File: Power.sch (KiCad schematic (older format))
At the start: 17 parts

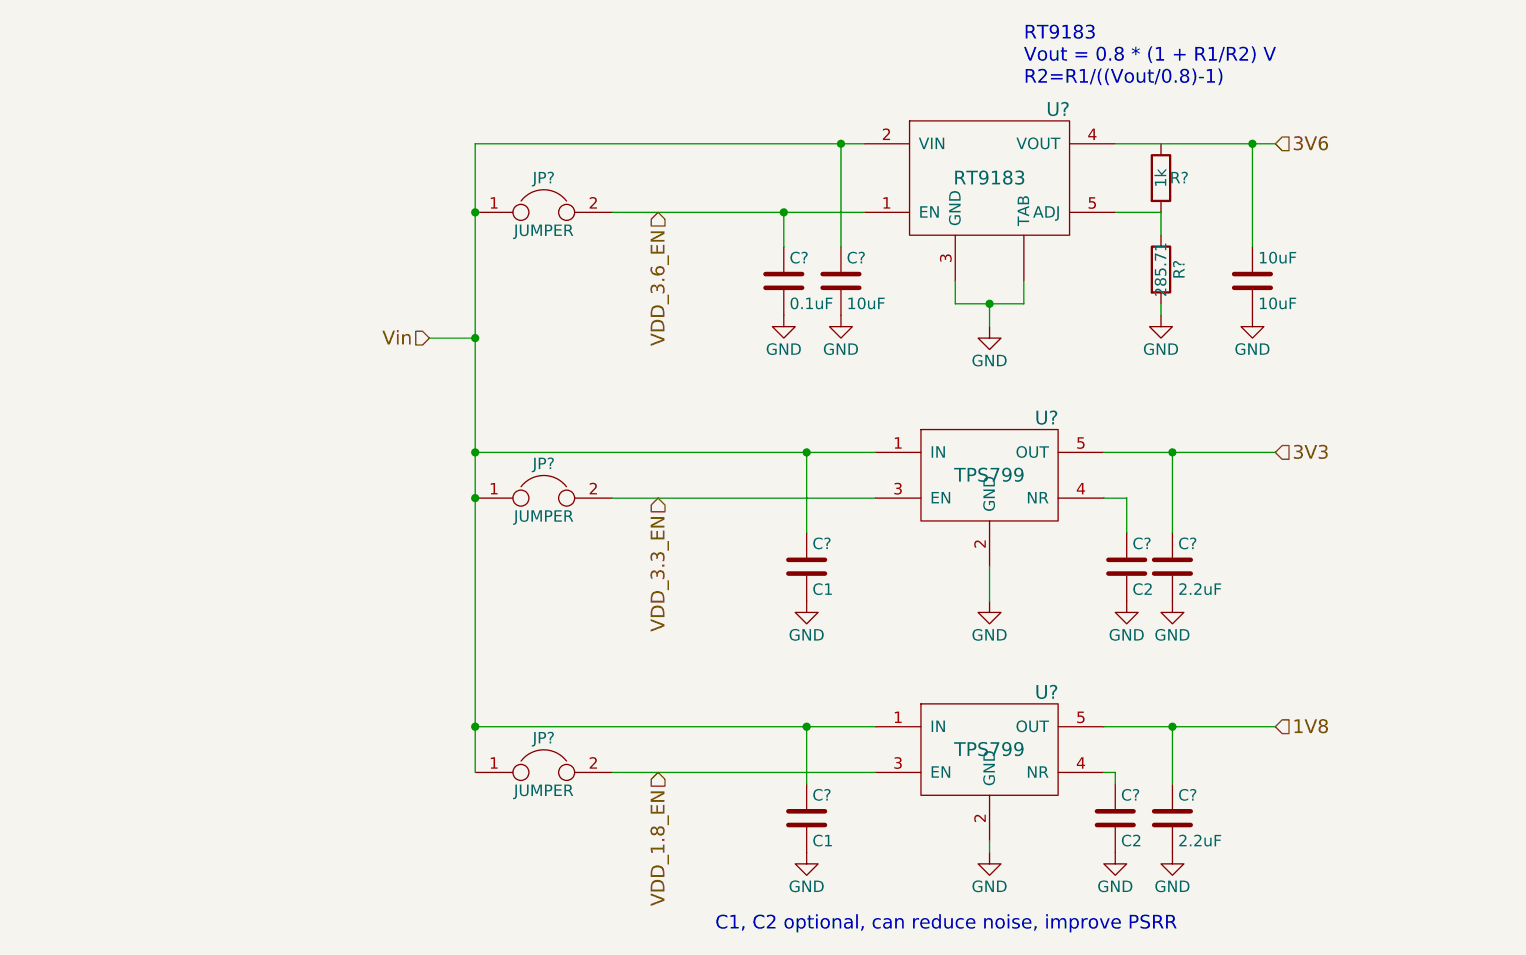
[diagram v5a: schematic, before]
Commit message: added switches for various option and nmos array to control status leds
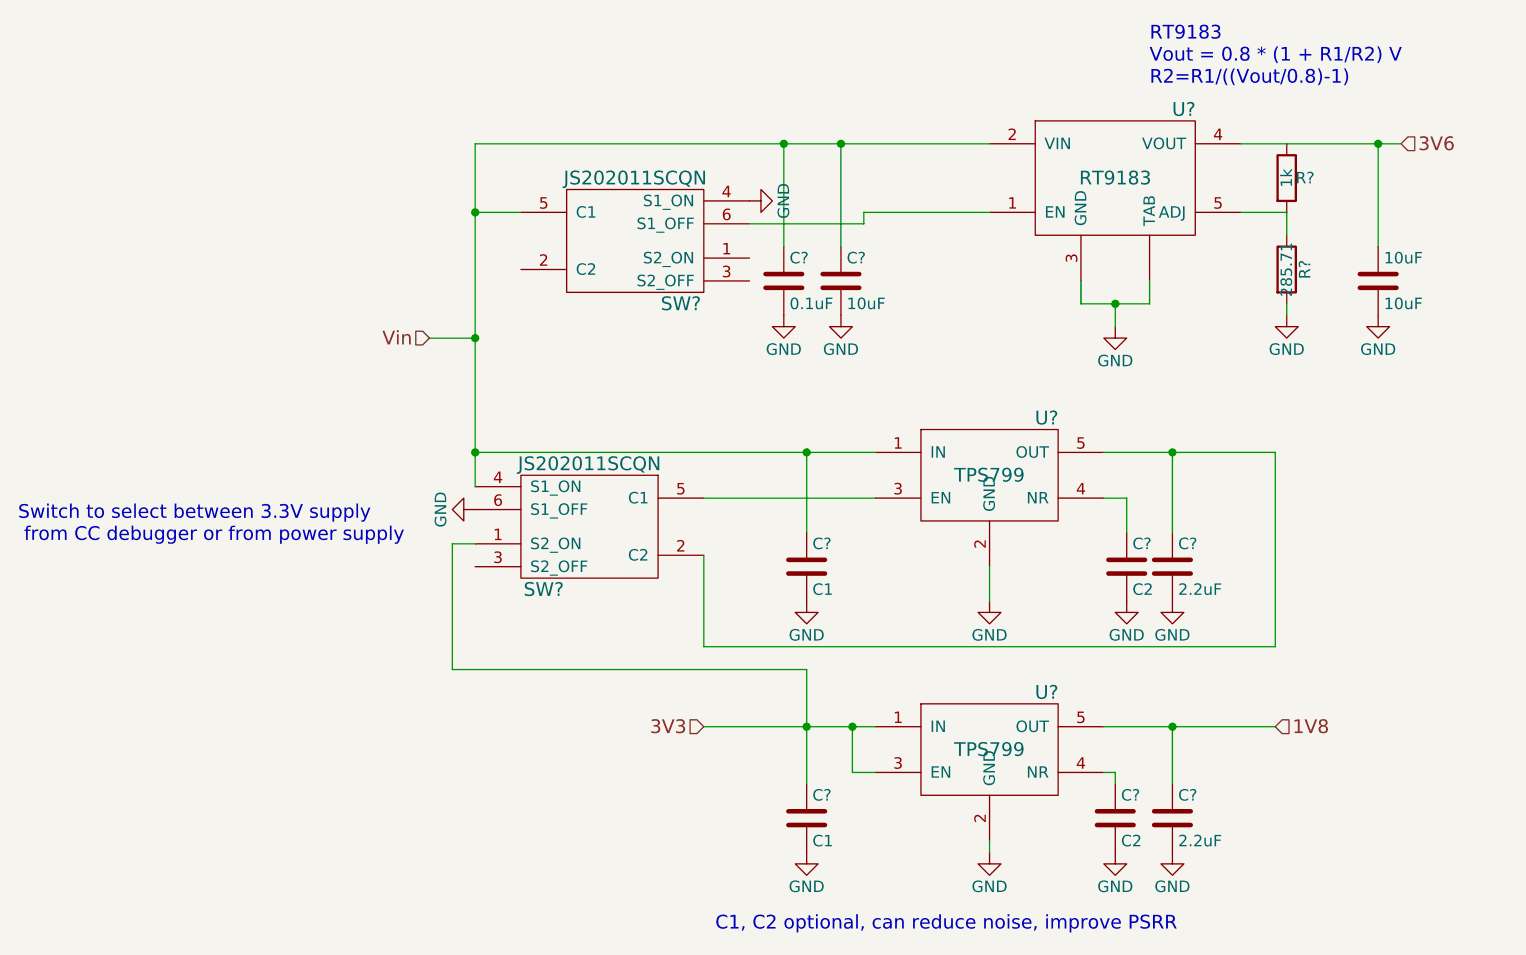
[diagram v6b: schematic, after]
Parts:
- removed JP? (x3): JUMPER, symbol JUMPER
- added SW? (x2): JS202011SCQN, symbol JS202011SCQN
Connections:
- net VDD_1.8_EN is gone; now on net 3V3: U?.3 (EN)
- net 3V3: now also C?.1, U?.1 (IN), SW?.1 (S2_ON); no longer C?.1, U?.5 (OUT)
- net GND: now also SW?.4 (S1_ON), SW?.6 (S1_OFF)
- net Vin: now also C?.1, SW?.4 (S1_ON), SW?.5 (C1); no longer C?.1, U?.1 (IN)
- net VDD_3.3_EN: no longer names the net of U?.3 (EN)
- net VDD_3.3_EN: now also SW?.5 (C1)
- net VDD_3.6_EN: no longer names the net of U?.1 (EN)
- net VDD_3.6_EN: now also SW?.6 (S1_OFF); no longer C?.1
- new net: C?.1, SW?.2 (C2), U?.5 (OUT)
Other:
- note added: "Switch to select between 3.3V supply\n from CC debugger or from power supply\n"
- moved on the sheet: 10uF, R?, U?
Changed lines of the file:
@@
 Text HLabel 3900 2850 0    60   Input ~ 0
 Vin
-Text HLabel 7600 3350 2    60   Input ~ 0
+Text HLabel 5100 4550 0    60   Input ~ 0
 3V3
-Text HLabel 7600 2000 2    60   Input ~ 0
+Text HLabel 8150 2000 2    60   Input ~ 0
 3V6
 Text HLabel 7600 4550 2    60   Input ~ 0
@@
 L RT9183 U?
 U 1 1 58770580
-P 6350 2150
-F 0 "U?" H 6650 2450 60  0000 C CNN
-F 1 "RT9183" H 6350 2150 60  0000 C CNN
-F 2 "" H 6350 2150 60  0001 C CNN
-F 3 "" H 6350 2150 60  0001 C CNN
-	1    6350 2150
+P 6900 2150
+F 0 "U?" H 7200 2450 60  0000 C CNN
+F 1 "RT9183" H 6900 2150 60  0000 C CNN
+F 2 "" H 6900 2150 60  0001 C CNN
+F 3 "" H 6900 2150 60  0001 C CNN
+	1    6900 2150
 	1    0    0    -1
 $EndComp
@@
 L GND #PWR?
 U 1 1 58770941
-P 6350 2800
-F 0 "#PWR?" H 6350 2550 50  0001 C CNN
-F 1 "GND" H 6350 2650 50  0000 C CNN
-F 2 "" H 6350 2800 50  0000 C CNN
-F 3 "" H 6350 2800 50  0000 C CNN
-	1    6350 2800
+P 6900 2800
+F 0 "#PWR?" H 6900 2550 50  0001 C CNN
+F 1 "GND" H 6900 2650 50  0000 C CNN
+F 2 "" H 6900 2800 50  0000 C CNN
+F 3 "" H 6900 2800 50  0000 C CNN
+	1    6900 2800
 	1    0    0    -1
 $EndComp
@@
 L C 10uF
 U 1 1 58770AC4
-P 7500 2600
-F 0 "10uF" H 7525 2700 50  0000 L CNN
-F 1 "10uF" H 7525 2500 50  0000 L CNN
-F 2 "" H 7538 2450 50  0000 C CNN
-F 3 "" H 7500 2600 50  0000 C CNN
-	1    7500 2600
+P 8050 2600
+F 0 "10uF" H 8075 2700 50  0000 L CNN
+F 1 "10uF" H 8075 2500 50  0000 L CNN
+F 2 "" H 8088 2450 50  0000 C CNN
+F 3 "" H 8050 2600 50  0000 C CNN
+	1    8050 2600
 	1    0    0    -1
 $EndComp
@@
 L GND #PWR?
 U 1 1 58770B93
-P 7500 2750
-F 0 "#PWR?" H 7500 2500 50  0001 C CNN
-F 1 "GND" H 7500 2600 50  0000 C CNN
-F 2 "" H 7500 2750 50  0000 C CNN
-F 3 "" H 7500 2750 50  0000 C CNN
-	1    7500 2750
+P 8050 2750
+F 0 "#PWR?" H 8050 2500 50  0001 C CNN
+F 1 "GND" H 8050 2600 50  0000 C CNN
+F 2 "" H 8050 2750 50  0000 C CNN
+F 3 "" H 8050 2750 50  0000 C CNN
+	1    8050 2750
 	1    0    0    -1
 $EndComp
@@
 L GND #PWR?
 U 1 1 58770BD7
-P 7100 2750
-F 0 "#PWR?" H 7100 2500 50  0001 C CNN
-F 1 "GND" H 7100 2600 50  0000 C CNN
-F 2 "" H 7100 2750 50  0000 C CNN
-F 3 "" H 7100 2750 50  0000 C CNN
-	1    7100 2750
+P 7650 2750
+F 0 "#PWR?" H 7650 2500 50  0001 C CNN
+F 1 "GND" H 7650 2600 50  0000 C CNN
+F 2 "" H 7650 2750 50  0000 C CNN
+F 3 "" H 7650 2750 50  0000 C CNN
+	1    7650 2750
 	1    0    0    -1
 $EndComp
@@
 L R R?
 U 1 1 58770EF4
-P 7100 2550
-F 0 "R?" V 7180 2550 50  0000 C CNN
-F 1 "285.71" V 7100 2550 50  0000 C CNN
-F 2 "" V 7030 2550 50  0000 C CNN
-F 3 "" H 7100 2550 50  0000 C CNN
-	1    7100 2550
+P 7650 2550
+F 0 "R?" V 7730 2550 50  0000 C CNN
+F 1 "285.71" V 7650 2550 50  0000 C CNN
+F 2 "" V 7580 2550 50  0000 C CNN
+F 3 "" H 7650 2550 50  0000 C CNN
+	1    7650 2550
 	1    0    0    -1
 $EndComp
@@
 L R R?
 U 1 1 58770EC5
-P 7100 2150
-F 0 "R?" H 7180 2150 50  0000 C CNN
-F 1 "1k" V 7100 2150 50  0000 C CNN
-F 2 "" V 7030 2150 50  0000 C CNN
-F 3 "" H 7100 2150 50  0000 C CNN
-	1    7100 2150
-	1    0    0    -1
-$EndComp
-Text Notes 6500 1750 0    60   ~ 0
+P 7650 2150
+F 0 "R?" H 7730 2150 50  0000 C CNN
+F 1 "1k" V 7650 2150 50  0000 C CNN
+F 2 "" V 7580 2150 50  0000 C CNN
+F 3 "" H 7650 2150 50  0000 C CNN
+	1    7650 2150
+	1    0    0    -1
+$EndComp
+Text Notes 7050 1750 0    60   ~ 0
 RT9183\nVout = 0.8 * (1 + R1/R2) V\nR2=R1/((Vout/0.8)-1)
 $Comp
@@
 Text Notes 5150 5450 0    60   ~ 0
 C1, C2 optional, can reduce noise, improve PSRR
-Text HLabel 4900 4750 3    60   Input ~ 0
-VDD_1.8_EN
-Text HLabel 4900 3550 3    60   Input ~ 0
-VDD_3.3_EN
-Text HLabel 4900 2300 3    60   Input ~ 0
-VDD_3.6_EN
-$Comp
-L JUMPER JP?
-U 1 1 587BADC1
-P 4400 2300
-F 0 "JP?" H 4400 2450 50  0000 C CNN
-F 1 "JUMPER" H 4400 2220 50  0000 C CNN
-F 2 "" H 4400 2300 50  0000 C CNN
-F 3 "" H 4400 2300 50  0000 C CNN
-	1    4400 2300
-	1    0    0    -1
-$EndComp
-$Comp
-L JUMPER JP?
-U 1 1 587BAE6A
-P 4400 3550
-F 0 "JP?" H 4400 3700 50  0000 C CNN
-F 1 "JUMPER" H 4400 3470 50  0000 C CNN
-F 2 "" H 4400 3550 50  0000 C CNN
-F 3 "" H 4400 3550 50  0000 C CNN
-	1    4400 3550
-	1    0    0    -1
-$EndComp
-$Comp
-L JUMPER JP?
-U 1 1 587BAFA3
-P 4400 4750
-F 0 "JP?" H 4400 4900 50  0000 C CNN
-F 1 "JUMPER" H 4400 4670 50  0000 C CNN
-F 2 "" H 4400 4750 50  0000 C CNN
-F 3 "" H 4400 4750 50  0000 C CNN
-	1    4400 4750
-	1    0    0    -1
-$EndComp
-Wire Wire Line
-	4100 2000 5800 2000
-Wire Wire Line
-	5700 2000 5700 2450
+$Comp
+L JS202011SCQN SW?
+U 1 1 587D58F9
+P 4800 2300
+F 0 "SW?" H 5000 1900 60  0000 C CNN
+F 1 "JS202011SCQN" H 4800 2450 60  0000 C CNN
+F 2 "" H 4800 2300 60  0000 C CNN
+F 3 "" H 4800 2300 60  0000 C CNN
+	1    4800 2300
+	1    0    0    -1
+$EndComp
+$Comp
+L JS202011SCQN SW?
+U 1 1 587D6D34
+P 4600 3550
+F 0 "SW?" H 4800 3150 60  0000 C CNN
+F 1 "JS202011SCQN" H 4600 3700 60  0000 C CNN
+F 2 "" H 4600 3550 60  0000 C CNN
+F 3 "" H 4600 3550 60  0000 C CNN
+	1    4600 3550
+	-1   0    0    -1
+$EndComp
+$Comp
+L GND #PWR?
+U 1 1 587D7AEC
+P 5300 2250
+F 0 "#PWR?" H 5300 2000 50  0001 C CNN
+F 1 "GND" H 5300 2100 50  0000 C CNN
+F 2 "" H 5300 2250 50  0000 C CNN
+F 3 "" H 5300 2250 50  0000 C CNN
+	1    5300 2250
+	0    -1   -1   0
+$EndComp
+$Comp
+L GND #PWR?
+U 1 1 587D7DE0
+P 4100 3600
+F 0 "#PWR?" H 4100 3350 50  0001 C CNN
+F 1 "GND" H 4100 3450 50  0000 C CNN
+F 2 "" H 4100 3600 50  0000 C CNN
+F 3 "" H 4100 3600 50  0000 C CNN
+	1    4100 3600
+	0    1    1    0
+$EndComp
+Wire Wire Line
+	4100 2000 6350 2000
 Connection ~ 5700 2000
 Wire Wire Line
-	4700 2300 5800 2300
-Wire Wire Line
-	5450 2300 5450 2450
-Connection ~ 5450 2300
-Wire Wire Line
-	6200 2600 6200 2700
-Wire Wire Line
-	6500 2600 6500 2700
-Wire Wire Line
-	6500 2700 6200 2700
-Wire Wire Line
-	6350 2700 6350 2800
-Connection ~ 6350 2700
-Wire Wire Line
-	6900 2000 7600 2000
-Wire Wire Line
-	7500 2000 7500 2450
-Connection ~ 7500 2000
-Wire Wire Line
-	6900 2300 7100 2300
-Wire Wire Line
-	7100 2300 7100 2400
-Wire Wire Line
-	7100 2750 7100 2700
-Wire Wire Line
-	4700 3550 5850 3550
+	6750 2600 6750 2700
+Wire Wire Line
+	7050 2600 7050 2700
+Wire Wire Line
+	7050 2700 6750 2700
+Wire Wire Line
+	6900 2700 6900 2800
+Connection ~ 6900 2700
+Wire Wire Line
+	7450 2000 8150 2000
+Wire Wire Line
+	8050 2000 8050 2450
+Connection ~ 8050 2000
+Wire Wire Line
+	7450 2300 7650 2300
+Wire Wire Line
+	7650 2300 7650 2400
+Wire Wire Line
+	7650 2750 7650 2700
 Wire Wire Line
 	6350 3850 6350 4000
@@
 	5550 3350 5550 3700
 Connection ~ 5550 3350
-Wire Wire Line
-	4100 4550 5850 4550
 Connection ~ 5550 4550
 Wire Wire Line
@@
 Connection ~ 7150 4550
 Wire Wire Line
-	4700 4750 5850 4750
-Wire Wire Line
 	6350 5050 6350 5100
-Wire Wire Line
-	5550 4800 5550 4550
-Wire Wire Line
-	4100 2000 4100 4750
-Connection ~ 4100 3550
 Wire Wire Line
 	4100 3350 5850 3350
 Connection ~ 4100 3350
-Connection ~ 4100 4550
 Connection ~ 4100 2300
 Wire Wire Line
 	4100 2850 3900 2850
 Connection ~ 4100 2850
+Wire Wire Line
+	5850 4750 5750 4750
+Wire Wire Line
+	5750 4750 5750 4550
+Connection ~ 5750 4550
+Wire Wire Line
+	4300 2300 4100 2300
+Wire Wire Line
+	5700 2450 5700 2000
+Wire Wire Line
+	5450 2450 5450 2000
+Connection ~ 5450 2000
+Wire Wire Line
+	5300 2350 5800 2350
+Wire Wire Line
+	5800 2350 5800 2300
+Wire Wire Line
+	7600 3350 7600 4200
+Wire Wire Line
+	5550 4300 5550 4800
+Wire Wire Line
+	5800 2300 6350 2300
+Wire Wire Line
+	5100 4550 5850 4550
+Text Notes 2100 3750 0    60   ~ 0
+Switch to select between 3.3V supply\n from CC debugger or from power supply\n
+Wire Wire Line
+	5850 3550 5100 3550
+Wire Wire Line
+	7600 4200 5100 4200
+Wire Wire Line
+	5100 4200 5100 3800
+Wire Wire Line
+	4100 2000 4100 3500
+Wire Wire Line
+	5550 4300 4000 4300
+Wire Wire Line
+	4000 4300 4000 3750
+Wire Wire Line
+	4000 3750 4100 3750
 $EndSCHEMATC
